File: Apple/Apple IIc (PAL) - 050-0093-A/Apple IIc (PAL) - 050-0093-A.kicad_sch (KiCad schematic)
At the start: 0 parts

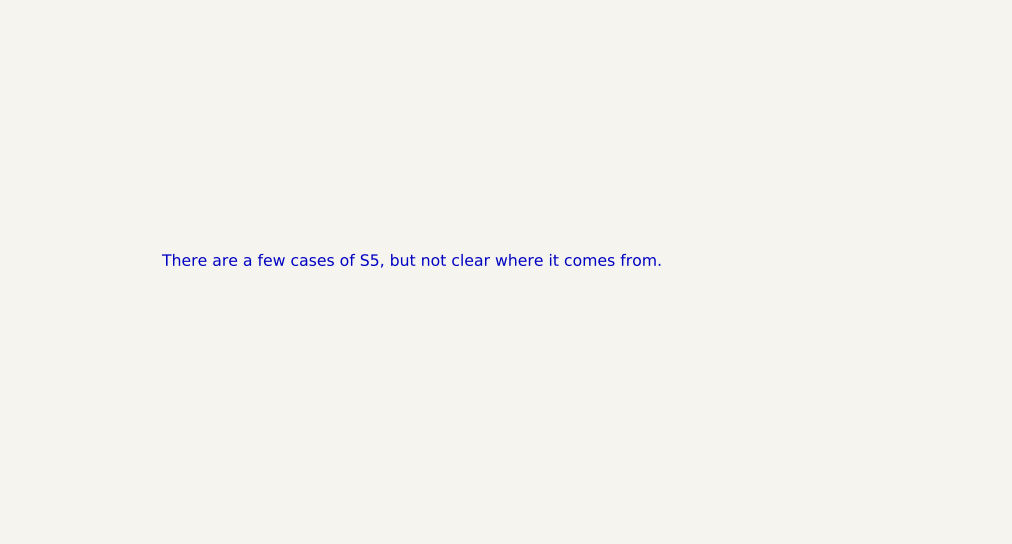
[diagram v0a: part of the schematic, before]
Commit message: Fixed S5 on CPU/ROM Page
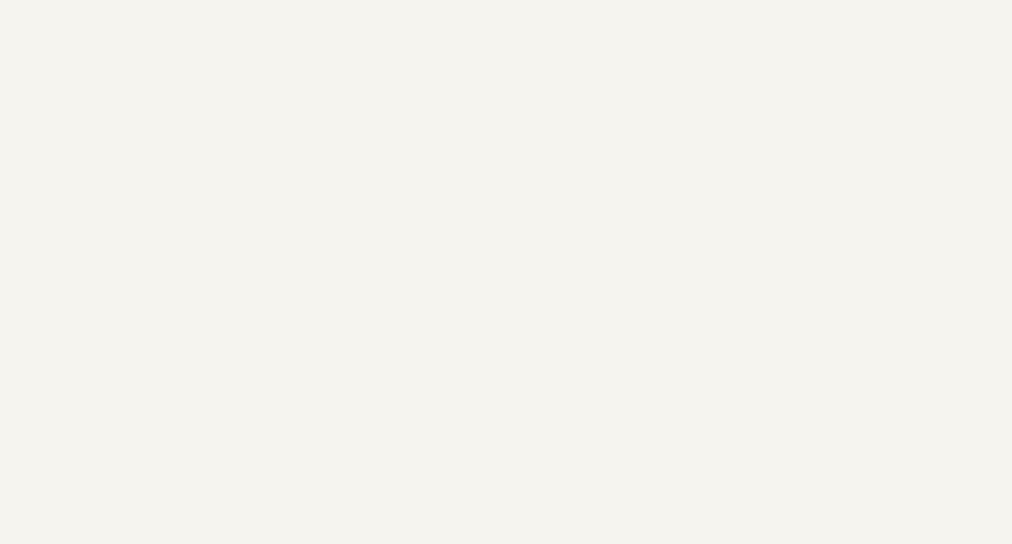
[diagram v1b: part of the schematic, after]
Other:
- note removed: "There are a few cases of S5, but not clear where it comes from."
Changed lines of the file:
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@@
-		)
-	)
-	(text "There are a few cases of S5, but not clear where it comes from."
-		(exclude_from_sim no)
-		(at 337.185 47.625 0)
-		(effects
-			(font
-				(size 1.27 1.27)
-			)
-			(justify left bottom)
 		)
 	)
